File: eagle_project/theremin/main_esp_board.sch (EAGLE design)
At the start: 7 parts

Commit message: updated main board
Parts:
- removed DAC: PCM5122PWRPW28-L, theremin:PCM5122PWRPW28-L
- added C1: 1 uF, Ilya_Teach:CAP
- added C13, C14, C2, C3, C4: 1uF, Ilya_Teach:CAP
- added J1: (no value), SparkFun-Connectors:CONN_07
- added LED1: BLUE, Ilya_Teach:LED0603
- added R7: (no value), rcl:R-US_0207/10
- added R8: 330R, Ilya_Teach:RES
- added U$1, U$2: SWITCH_BTN_NO, Ilya_Teach:SWITCH_BTN_NO
- added U$6: VREG-3V3, Ilya_Teach:VREG-3V3
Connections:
- new net -VDD5V0: MUX.VEE, REGULATOR.VOUT
- new net ANALOG_IN: MUX.CH0_IN/OUT
- new net BCLK: ESP32.GPIO27, J1.2
- new net DIGITAL_IN: MUX.CH1_IN/OUT
- new net DIN: ESP32.GPIO26, J1.3
- new net EN: C4.1, ESP32.EN, U$2.1
- new net GAIN: J1.4, R7.1
- new net GND: C13.2, C14.2, C2.2, C4.2, ESP32.GND2, ESP32.GND4, ESP32.GND5, J1.6, LED1.C, MUX.INH, MUX.VSS, R7.2, REGULATOR.GND, U$1.2, U$2.2, U$6.GND
- new net IO0: C2.1, ESP32.GPIO0, U$1.1
- new net LRC: ESP32.GPIO14, J1.1
- new net MUX_OUT: MUX.COM_OUT/IN
- new net N$1: C1.1, REGULATOR.C1+
- new net N$2: C1.2, REGULATOR.C1-
- new net N$8: LED1.A, R8.1
- new net SD: J1.5
- new net SEL: MUX.A
- new net VDD3V0: C14.1, ESP32.3.3V, R8.2, U$6.OUT@2, U$6.OUT@4
- new net VDD5V0: C13.1, J1.7, MUX.VDD, REGULATOR.EN, REGULATOR.VIN, U$6.IN
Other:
- moved on the sheet: AMPLIFIER, DIGIPOT1, DIGIPOT2, MUX, REGULATOR

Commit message: updated board
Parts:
- added C16: 0.1uF, Ilya_Teach:CAP
- added C5: 1uF, Ilya_Teach:CAP
- added J2: FEMALE 2x3, SparkFun-Connectors:CONN_03X2FEMALE
- added J3: (no value), SparkFun-Connectors:CONN_02
- added J4, J5: (no value), SparkFun-Connectors:CONN_04PTH
- added R9: 10K, Ilya_Teach:RES
- added U$3: SWITCH_BTN_NO, Ilya_Teach:SWITCH_BTN_NO
- added U$5: BARREL_2.1MMSMT, Ilya_Teach:BARREL_2.1MMSMT
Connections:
- removed net VDD3V0: C14.1, ESP32.3.3V, R8.2, U$6.OUT@2, U$6.OUT@4
- new net AMP+: AMPLIFIER.IN+, J3.2
- new net AMP-: AMPLIFIER.IN-, J3.1
- new net ECHO_FREQ: ESP32.GPIO39, J4.2
- new net ECHO_VOL: ESP32.GPIO34, J5.2
- new net N$3: ESP32.EN, R9.2
- new net RX: ESP32.RX, J2.2
- new net SPK+: AMPLIFIER.VO+
- new net SPK-: AMPLIFIER.VO-
- new net TRIG_FREQ: ESP32.GPIO32, J4.3
- new net TRIG_VOL: ESP32.GPIO33, J5.3
- new net TX: ESP32.TX, J2.4
- new net VDD3V3: C14.1, C16.1, ESP32.3.3V, R8.2, R9.1, U$6.OUT@2, U$6.OUT@4
- net EN: no longer ESP32.EN
- net GND: now also AMPLIFIER.EPAD, AMPLIFIER.GND, C16.2, C5.2, J2.3, J4.1, J5.1, U$3.2, U$5.GND, U$5.GNDBREAK; no longer R7.2
- net SD: now also C5.1, U$3.1
- net VDD5V0: now also AMPLIFIER.!SHUTDOWN, AMPLIFIER.VDD, J2.1, J4.4, J5.4, R7.2, U$5.PWR
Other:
- moved on the sheet: J1, MUX, R7

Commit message: digipot code + schematic
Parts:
- removed J2: FEMALE 2x3, SparkFun-Connectors:CONN_03X2FEMALE
- removed MUX: CD4051BM96, CD4051BM96:CD4051BM96
- removed R9: 10K, Ilya_Teach:RES
- added C10, C12, C17, C22, C8: 1uF, Ilya_Teach:CAP
- added C11, C15, C20, C21, C6, C7, C9: 0.1uF, Ilya_Teach:CAP
- added C18, C19: 2.2 uF, Ilya_Teach:CAP
- added C23: 0.22uF, Ilya_Teach:CAP
- added C_X1, C_X2: 0.16uF, SparkFun-Connectors:CONN_02
- added J6: (no value), SparkFun-Connectors:CONN_04X2
- added MUX1, MUX_POSITIVE: CD4051BM96, CD4051BM96:CD4051BM96
- added R1: (no value), rcl:R-US_0207/10
- C2, C4, C5: value 1uF -> 0.1uF
- C3: value 1uF -> 22uF
- J3: value (none) -> SPEAKER
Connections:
- removed net AMP+: AMPLIFIER.IN+, J3.2
- removed net AMP-: AMPLIFIER.IN-, J3.1
- removed net ANALOG_IN: MUX.CH0_IN/OUT
- removed net DIGITAL_IN: MUX.CH1_IN/OUT
- removed net MUX_OUT: MUX.COM_OUT/IN
- new net AMPLIFIER_+: C_X1.1, MUX_POSITIVE.COM_OUT/IN
- new net AMPLIFIER_-: C_X2.1, MUX1.COM_OUT/IN
- new net ANALOG+: J6.6, MUX_POSITIVE.CH1_IN/OUT
- new net ANALOG-: J6.5, MUX1.CH1_IN/OUT
- new net DAC+: MUX_POSITIVE.CH0_IN/OUT
- new net DAC-: MUX1.CH0_IN/OUT
- new net IN+: AMPLIFIER.IN+, DIGIPOT2.A
- new net IN-: AMPLIFIER.IN-, DIGIPOT1.A
- new net N$6: C_X1.2, DIGIPOT2.W
- new net N$7: C_X2.2, DIGIPOT1.W
- new net SCL: DIGIPOT1.SCL, DIGIPOT2.SCL
- new net SDA: DIGIPOT1.SDA, DIGIPOT2.SDA
- net -VDD5V0: now also C10.1, C11.1, C12.1, C19.1, C9.1, J6.2, MUX1.VEE, MUX_POSITIVE.VEE; no longer MUX.VEE
- net EN: now also C6.1, ESP32.EN, R1.1
- net GND: now also C10.2, C11.2, C12.2, C15.2, C17.2, C18.2, C19.2, C20.2, C21.2, C22.1, C23.2, C3.2, C6.2, C7.2, C8.2, C9.2, DIGIPOT1.AD0, DIGIPOT1.GND, DIGIPOT2.GND, J6.3, MUX1.INH, MUX1.VSS, MUX_POSITIVE.INH, MUX_POSITIVE.VSS; no longer J2.3, MUX.INH, MUX.VSS
- net N$3: now also AMPLIFIER.BYPASS, C23.1; no longer ESP32.EN, R9.2
- net RX: now also J6.7; no longer J2.2
- net SEL: now also MUX1.A, MUX_POSITIVE.A; no longer MUX.A
- net SPK+: now also J3.1
- net SPK-: now also J3.2
- net TX: now also J6.8; no longer J2.4
- net VDD3V3: now also C3.1, J6.4, R1.2; no longer R9.1
- net VDD5V0: now also C15.1, C17.1, C18.1, C20.1, C21.1, C22.2, C7.1, C8.1, DIGIPOT1.VDD, DIGIPOT2.AD0, DIGIPOT2.VDD, J6.1, MUX1.VDD, MUX_POSITIVE.VDD; no longer J2.1, MUX.VDD
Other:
- note added: "(input capacitor -- likely unpopulated)"
- note added: "Analog Input + Programming"
- note added: "Buttons"
- note added: "ESP"
- note added: "Etc."
- note added: "Headers"
- note added: "MAX98357 Connectors"
- note added: "MUXes"
- note added: "Output Stage"
- note added: "Regulators"
- note added: "Ultrasonic Sensors"
- moved on the sheet: AMPLIFIER, C1, C13, C14, C16, C2, C3, C4, C5, DIGIPOT1, DIGIPOT2, J1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

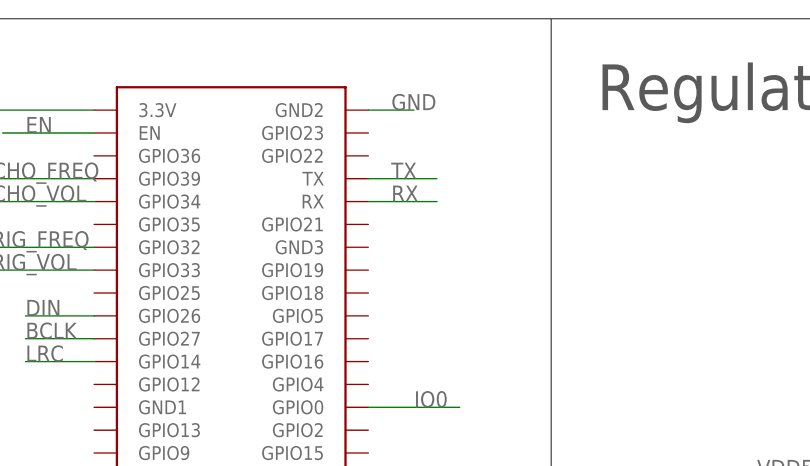
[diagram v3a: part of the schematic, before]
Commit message: added I2C connections
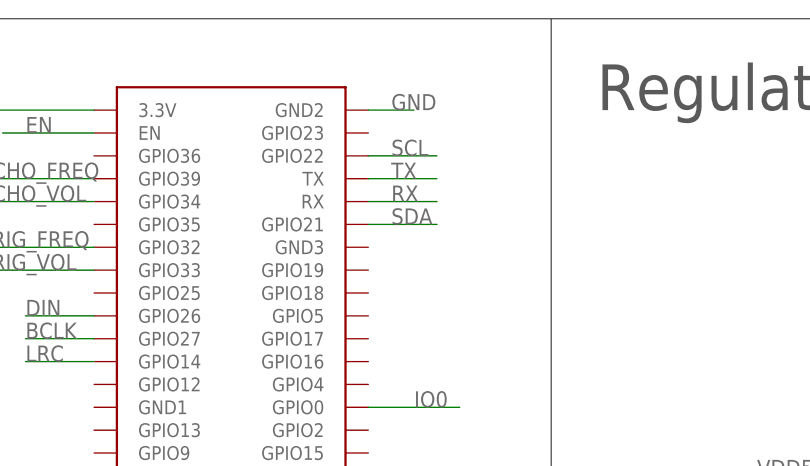
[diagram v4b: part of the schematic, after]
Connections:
- net SCL: now also ESP32.GPIO22
- net SDA: now also ESP32.GPIO21
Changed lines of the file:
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@@
 <label x="-165.1" y="154.94" size="1.778" layer="95"/>
+</segment>
+<segment>
+<pinref part="ESP32" gate="G$1" pin="GPIO22"/>
+<wire x1="101.6" y1="299.72" x2="109.22" y2="299.72" width="0.1524" layer="91"/>
+<label x="104.14" y="299.72" size="1.778" layer="95"/>
 </segment>
 </net>
@@
 <label x="-114.3" y="154.94" size="1.778" layer="95"/>
 </segment>
+<segment>
+<pinref part="ESP32" gate="G$1" pin="GPIO21"/>
+<wire x1="101.6" y1="292.1" x2="109.22" y2="292.1" width="0.1524" layer="91"/>
+<label x="104.14" y="292.1" size="1.778" layer="95"/>
+</segment>
 </net>
